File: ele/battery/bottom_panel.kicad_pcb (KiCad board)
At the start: 2 copper layers, 86.7 x 87.2 mm, 28 parts, among them J14 mech, J15 mech, J16 B1_P_tans_b, J17 B1_M_tans_b, J18 B2_P_tans_b, J19 B2_M_tans_b, J20 B1_P_b, J21 B1_P_a, J22 B1_M_a, J23 B1_M_b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

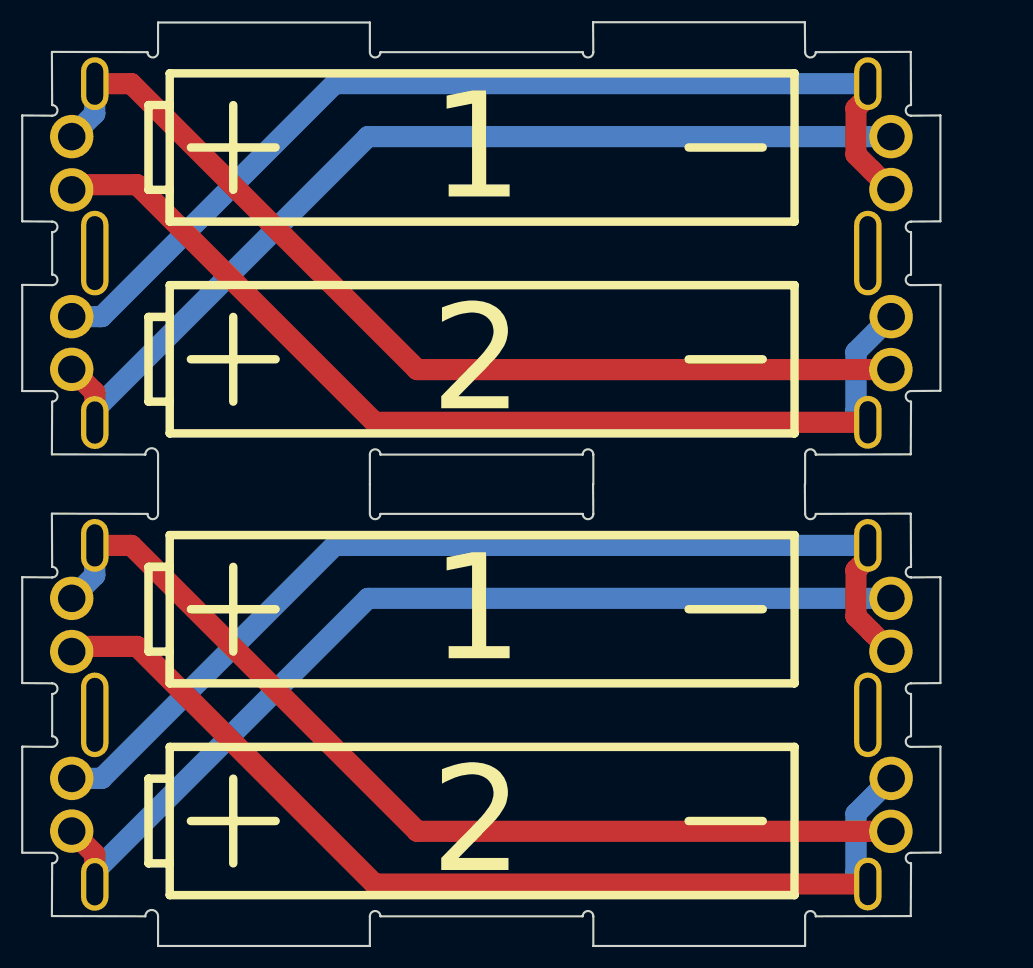
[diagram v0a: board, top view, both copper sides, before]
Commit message: ele: Update battery panels
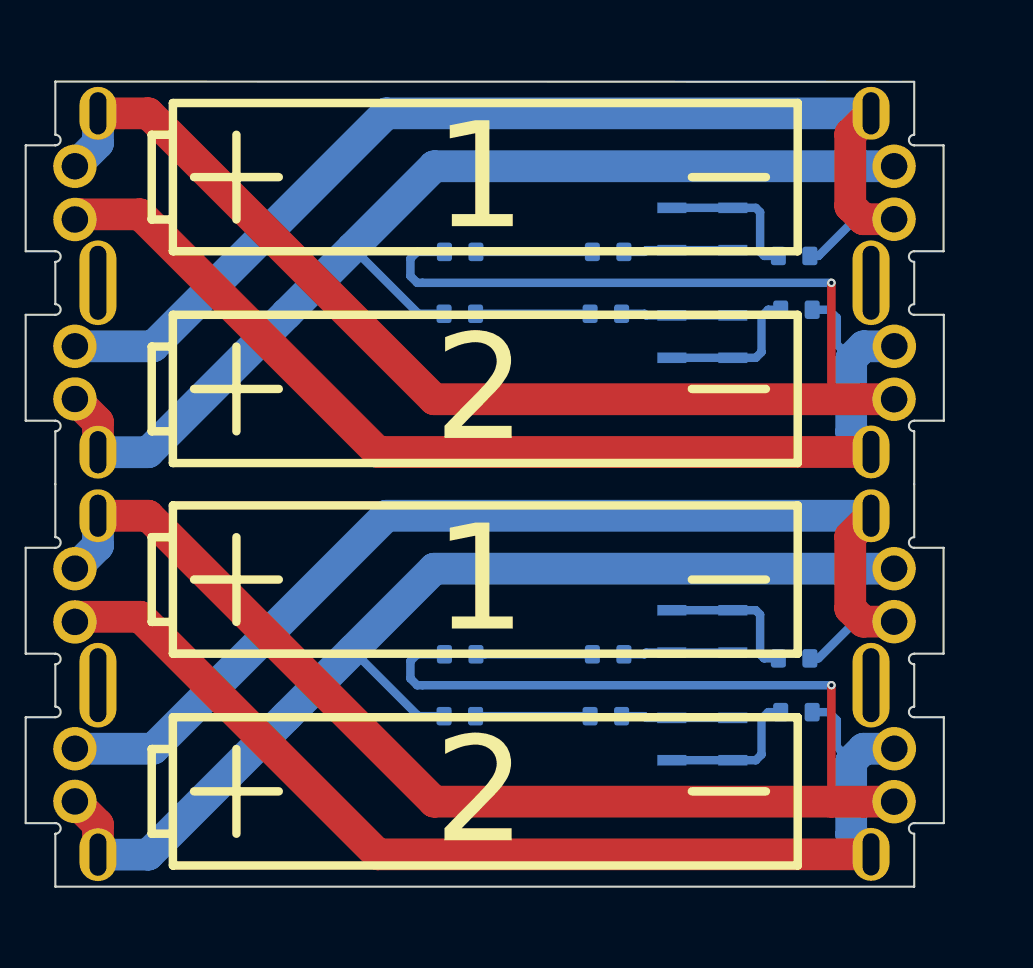
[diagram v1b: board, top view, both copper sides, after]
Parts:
- added D1: D_Zener_2V, Diode_SMD:D_1206_3216Metric_Pad1.42x1.75mm_HandSolder, B.Cu at (151.4, 137.7)
- added D1: D_Zener_2V, Diode_SMD:D_1206_3216Metric_Pad1.42x1.75mm_HandSolder, B.Cu at (151.4, 99.7)
- added D2: D_Zener_2V, Diode_SMD:D_1206_3216Metric_Pad1.42x1.75mm_HandSolder, B.Cu at (151.4, 131.9)
- added D2: D_Zener_2V, Diode_SMD:D_1206_3216Metric_Pad1.42x1.75mm_HandSolder, B.Cu at (151.4, 93.9)
- added LED1: LED_RED, LED_SMD:LED_1206_3216Metric_Pad1.42x1.75mm_HandSolder, B.Cu at (165.2, 137.7)
- added LED1: LED_RED, LED_SMD:LED_1206_3216Metric_Pad1.42x1.75mm_HandSolder, B.Cu at (165.2, 99.7)
- added LED2: LED_RED, LED_SMD:LED_1206_3216Metric_Pad1.42x1.75mm_HandSolder, B.Cu at (165.4, 131.9)
- added LED2: LED_RED, LED_SMD:LED_1206_3216Metric_Pad1.42x1.75mm_HandSolder, B.Cu at (165.4, 93.9)
- added R1: R, Resistor_SMD:R_1206_3216Metric_Pad1.42x1.75mm_HandSolder, B.Cu at (183.2, 137.3)
- added R1: R, Resistor_SMD:R_1206_3216Metric_Pad1.42x1.75mm_HandSolder, B.Cu at (183.2, 99.3)
- added R2: R, Resistor_SMD:R_1206_3216Metric_Pad1.42x1.75mm_HandSolder, B.Cu at (183.0, 132.2)
- added R2: R, Resistor_SMD:R_1206_3216Metric_Pad1.42x1.75mm_HandSolder, B.Cu at (183.0, 94.2)
- added SW1: SW_Push, Button_Switch_SMD:SW_SPST_EVQP0, B.Cu at (174.3, 139.9)
- added SW1: SW_Push, Button_Switch_SMD:SW_SPST_EVQP0, B.Cu at (174.3, 101.9)
- added SW2: SW_Push, Button_Switch_SMD:SW_SPST_EVQP0, B.Cu at (174.3, 129.7)
- added SW2: SW_Push, Button_Switch_SMD:SW_SPST_EVQP0, B.Cu at (174.3, 91.7)
- J14 (x2): moved to B.Cu
- moved J21 2.82 mm to (192.4, 107.8)
- moved J22 2.82 mm to (192.4, 90.8)
- moved J24 2.82 mm to (192.4, 85.8)
- moved J26 2.82 mm to (192.4, 102.8)
- moved J14 2.82 mm to (117.2, 96.8)
- moved J16 2.82 mm to (117.2, 80.8)
- moved J18 2.82 mm to (117.2, 112.8)
- moved J20 2.82 mm to (115.0, 85.8)
- moved J23 2.82 mm to (115.0, 102.8)
- moved J25 2.82 mm to (115.0, 145.8)
- moved J15 2.82 mm to (190.2, 96.8)
- moved J17 2.82 mm to (190.2, 80.8)
- moved J19 2.82 mm to (190.2, 150.8)
- moved J24 2.82 mm to (192.4, 123.8)
- moved J16 2.82 mm to (117.2, 118.8)
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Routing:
- net /B1+: track 184.5 -> 296.8 mm, vias 0 -> 2
- net Net-(R2-Pad2): track 0.00 -> 28.3 mm
- net Net-(R1-Pad2): track 0.00 -> 28.3 mm
- net /B1-: track 192.2 -> 215.8 mm
- net Net-(D2-Pad2): track 0.00 -> 22.0 mm
- net Net-(D1-Pad2): track 0.00 -> 21.6 mm
- net Net-(LED1-Pad1): track 0.00 -> 21.1 mm
- net /B2+: track 186.0 -> 207.0 mm
- net Net-(LED2-Pad1): track 0.00 -> 20.7 mm
- net /B2-: track 193.0 -> 212.5 mm
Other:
- board size 86.7 x 87.2 mm -> 86.7 x 76 mm
- board text added: "B1"
- board text added: "B2"
- board text added: "Mickoflus Battery Pack v0.3 04/2019 RobotikaBrno.cz github:roboticsbrno/ RB3201-RBControl"
- board text removed: "Mickoflus Batterry Pack v0.1 12/2018 RobotikaBrno.cz"

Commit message: ele: Update battery panels
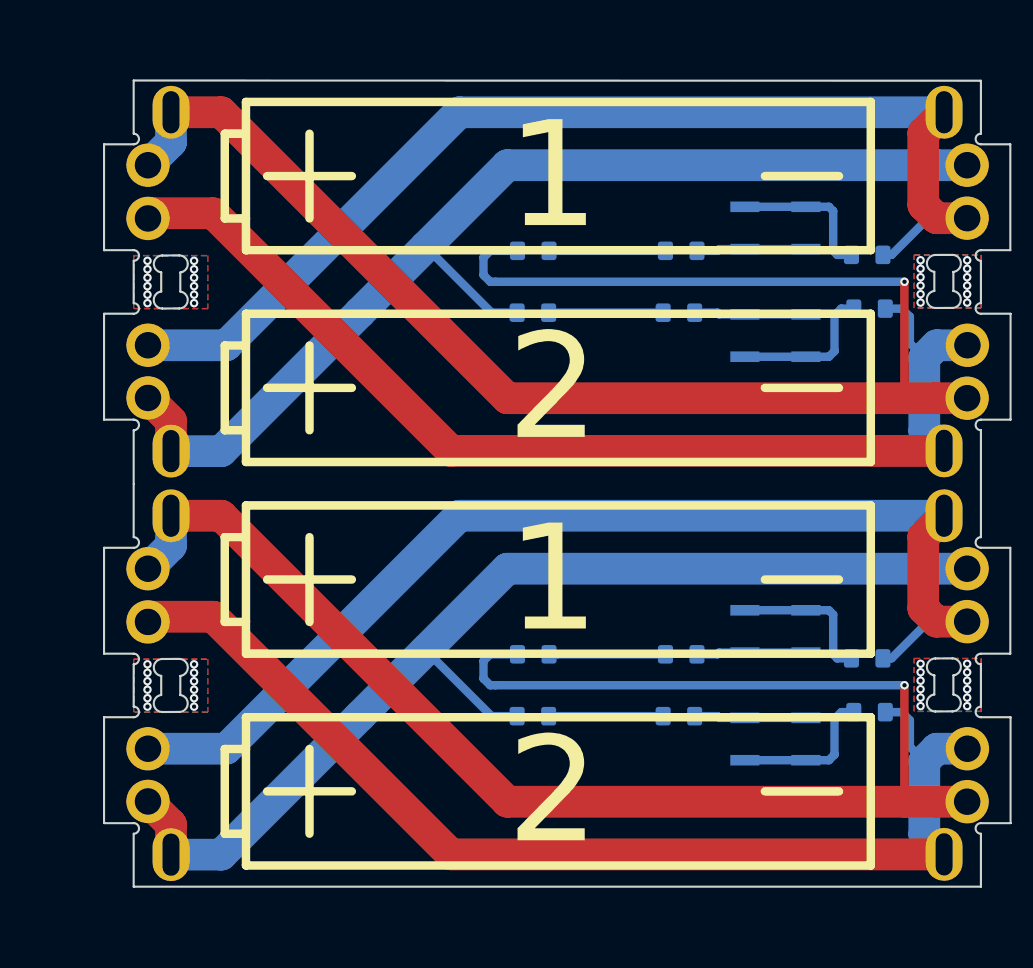
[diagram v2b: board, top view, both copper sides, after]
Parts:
- removed J14 (x2), J15 (x2): mech, yaqwsx:slot_1.8x5
- moved D1 6.90 mm to (158.3, 99.6)
- moved D2 6.90 mm to (158.3, 93.8)
- moved J16 6.90 mm to (124.1, 80.7)
- moved J17 6.90 mm to (197.1, 80.7)
- moved J18 6.90 mm to (124.1, 112.7)
- moved J19 6.90 mm to (197.1, 112.7)
- moved J20 6.90 mm to (122.0, 85.7)
- moved J21 6.90 mm to (199.3, 107.7)
- moved J22 6.90 mm to (199.3, 90.7)
- moved J23 6.90 mm to (122.0, 102.7)
- moved J24 6.90 mm to (199.3, 85.7)
- moved J25 6.90 mm to (122.0, 107.7)
- moved J27 6.90 mm to (122.0, 90.7)
- moved LED1 6.90 mm to (172.1, 99.6)
- moved LED2 6.90 mm to (172.3, 93.8)
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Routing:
- net (no net): vias 0 -> 48
- added copper zone on B.Cu, net (none)
- added copper zone on F.Cu, net (none)
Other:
- board size 86.7 x 76 mm -> 85.6 x 76.1 mm
- board text added: "Mickoflus Battery Pack v0.4 04/2019 RobotikaBrno.cz github:roboticsbrno/ RB3201-RBControl"
- board text removed: "Mickoflus Battery Pack v0.3 04/2019 RobotikaBrno.cz github:roboticsbrno/ RB3201-RBControl"
